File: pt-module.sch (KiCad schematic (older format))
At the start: 0 parts

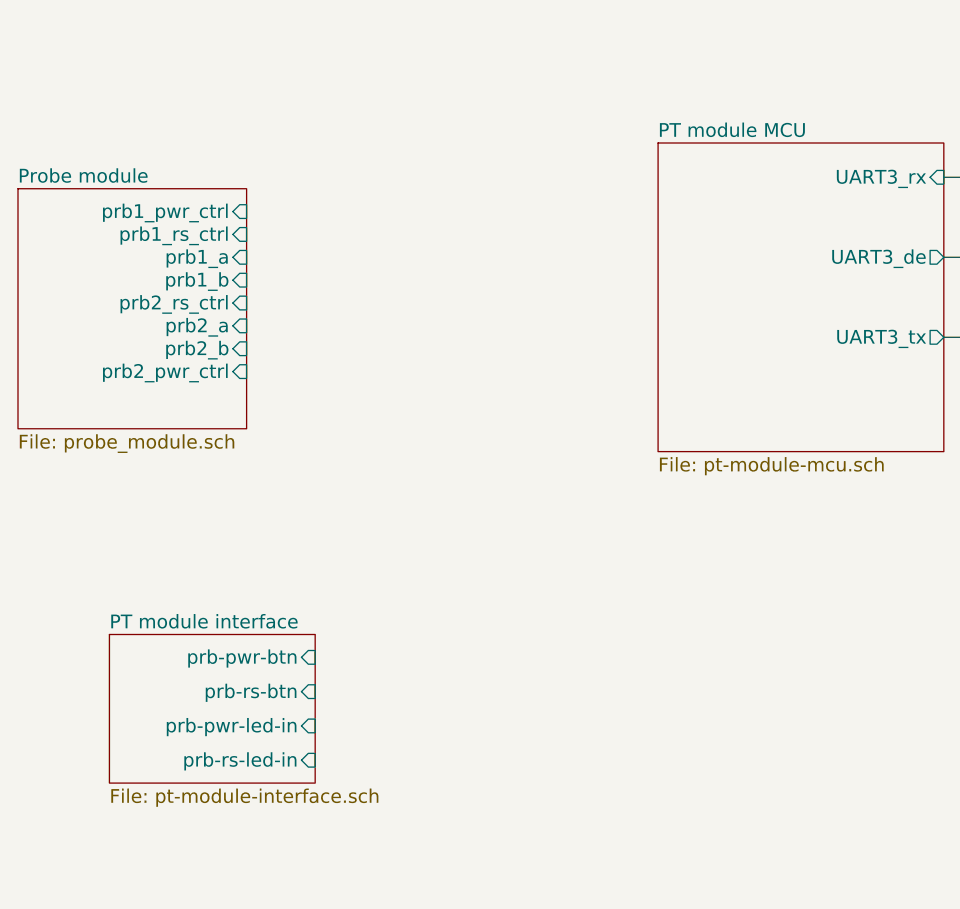
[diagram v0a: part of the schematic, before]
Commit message: add vaisala bus
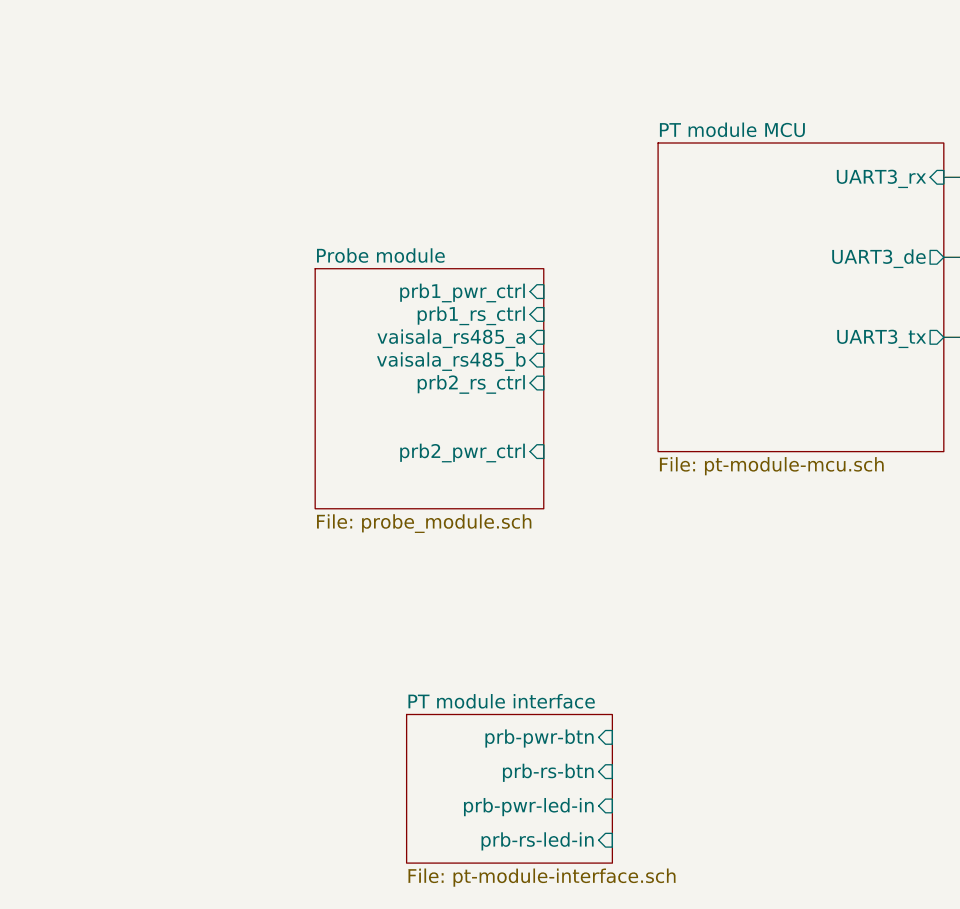
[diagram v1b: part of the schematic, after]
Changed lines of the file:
@@
 	6500 2100 7200 2100
 $Sheet
-S 1300 3000 1000 1050
+S 2600 3350 1000 1050
 U 598183C5
 F0 "Probe module" 60
 F1 "probe_module.sch" 60
-F2 "prb1_pwr_ctrl" I R 2300 3100 60
-F3 "prb1_rs_ctrl" I R 2300 3200 60
-F4 "prb1_a" I R 2300 3300 60
-F5 "prb1_b" I R 2300 3400 60
-F6 "prb2_rs_ctrl" I R 2300 3500 60
-F7 "prb2_a" I R 2300 3600 60
-F8 "prb2_b" I R 2300 3700 60
-F9 "prb2_pwr_ctrl" I R 2300 3800 60
+F2 "prb1_pwr_ctrl" I R 3600 3450 60
+F3 "prb1_rs_ctrl" I R 3600 3550 60
+F4 "prb2_rs_ctrl" I R 3600 3850 60
+F5 "prb2_pwr_ctrl" I R 3600 4150 60
+F6 "vaisala_rs485_a" I R 3600 3650 60
+F7 "vaisala_rs485_b" I R 3600 3750 60
 $EndSheet
 $Sheet
-S 1700 4950 900  650
+S 3000 5300 900  650
 U 59819805
 F0 "PT module interface" 60
 F1 "pt-module-interface.sch" 60
-F2 "prb-pwr-btn" I R 2600 5050 60
-F3 "prb-rs-btn" I R 2600 5200 60
-F4 "prb-pwr-led-in" I R 2600 5350 60
-F5 "prb-rs-led-in" I R 2600 5500 60
+F2 "prb-pwr-btn" I R 3900 5400 60
+F3 "prb-rs-btn" I R 3900 5550 60
+F4 "prb-pwr-led-in" I R 3900 5700 60
+F5 "prb-rs-led-in" I R 3900 5850 60
 $EndSheet
 $EndSCHEMATC

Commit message: add connectors
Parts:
- added J?: M12 out, symbol CONN_01X05
- added J? (x2): Ethercon out, symbol CONN_01X08
- added J?: M12 in, symbol CONN_01X05
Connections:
- new net GND: J?.2 (P2), J?.2 (P2), J?.8 (P8), J?.8 (P8)
- new net VCC: J?.1 (P1), J?.1 (P1), J?.1 (P1), J?.1 (P1), J?.2 (P2), J?.2 (P2), J?.3 (P3), J?.3 (P3)
- new net intermodule_rs485_a: J?.6 (P6), J?.6 (P6)
- new net intermodule_rs485_b: J?.7 (P7), J?.7 (P7)
- new net vaisala_rs485_a: J?.3 (P3), J?.3 (P3), J?.4 (P4), J?.4 (P4)
- new net vaisala_rs485_b: J?.4 (P4), J?.4 (P4), J?.5 (P5), J?.5 (P5)
- no-connect marks 0 -> 2
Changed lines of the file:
@@
 $EndDescr
 $Sheet
-S 7150 3350 1750 900
+S 2150 1200 1750 900
 U 5979DB00
 F0 "PT Module Power" 60
 F1 "pt-module-power.sch" 60
-F2 "PWREN" I L 7150 3625 60
+F2 "PWREN" I L 2150 1475 60
 $EndSheet
 $Sheet
@@
 F5 "prb-rs-led-in" I R 3900 5850 60
 $EndSheet
+$Comp
+L CONN_01X05 J?
+U 1 1 59820FE7
+P 10850 1050
+F 0 "J?" H 10850 1350 50  0000 C CNN
+F 1 "M12 out" V 10950 1050 50  0000 C CNN
+F 2 "" H 10850 1050 50  0001 C CNN
+F 3 "" H 10850 1050 50  0001 C CNN
+	1    10850 1050
+	1    0    0    -1
+$EndComp
+$Comp
+L VCC #PWR?
+U 1 1 598232AF
+P 10650 850
+F 0 "#PWR?" H 10650 700 50  0001 C CNN
+F 1 "VCC" H 10650 1000 50  0000 C CNN
+F 2 "" H 10650 850 50  0001 C CNN
+F 3 "" H 10650 850 50  0001 C CNN
+	1    10650 850
+	0    -1   -1   0
+$EndComp
+$Comp
+L GND #PWR?
+U 1 1 59823366
+P 10650 950
+F 0 "#PWR?" H 10650 700 50  0001 C CNN
+F 1 "GND" H 10650 800 50  0000 C CNN
+F 2 "" H 10650 950 50  0001 C CNN
+F 3 "" H 10650 950 50  0001 C CNN
+	1    10650 950
+	0    1    1    0
+$EndComp
+Text Label 10650 1050 2    60   ~ 0
+vaisala_rs485_a
+Text Label 10650 1150 2    60   ~ 0
+vaisala_rs485_b
+NoConn ~ 10650 1250
+$Comp
+L CONN_01X08 J?
+U 1 1 59829448
+P 10850 1900
+F 0 "J?" H 10850 2350 50  0000 C CNN
+F 1 "Ethercon out" V 10950 1900 50  0000 C CNN
+F 2 "" H 10850 1900 50  0001 C CNN
+F 3 "" H 10850 1900 50  0001 C CNN
+	1    10850 1900
+	1    0    0    -1
+$EndComp
+$Comp
+L CONN_01X05 J?
+U 1 1 5982A52D
+P 800 1250
+F 0 "J?" H 800 1550 50  0000 C CNN
+F 1 "M12 in" V 900 1250 50  0000 C CNN
+F 2 "" H 800 1250 50  0001 C CNN
+F 3 "" H 800 1250 50  0001 C CNN
+	1    800  1250
+	-1   0    0    1
+$EndComp
+$Comp
+L VCC #PWR?
+U 1 1 5982A533
+P 1000 1450
+F 0 "#PWR?" H 1000 1300 50  0001 C CNN
+F 1 "VCC" H 1000 1600 50  0000 C CNN
+F 2 "" H 1000 1450 50  0001 C CNN
+F 3 "" H 1000 1450 50  0001 C CNN
+	1    1000 1450
+	0    1    1    0
+$EndComp
+$Comp
+L GND #PWR?
+U 1 1 5982A539
+P 1000 1350
+F 0 "#PWR?" H 1000 1100 50  0001 C CNN
+F 1 "GND" H 1000 1200 50  0000 C CNN
+F 2 "" H 1000 1350 50  0001 C CNN
+F 3 "" H 1000 1350 50  0001 C CNN
+	1    1000 1350
+	0    -1   -1   0
+$EndComp
+Text Label 1000 1250 0    60   ~ 0
+vaisala_rs485_a
+Text Label 1000 1150 0    60   ~ 0
+vaisala_rs485_b
+NoConn ~ 1000 1050
+$Comp
+L VCC #PWR?
+U 1 1 59839AE4
+P 10650 1550
+F 0 "#PWR?" H 10650 1400 50  0001 C CNN
+F 1 "VCC" H 10650 1700 50  0000 C CNN
+F 2 "" H 10650 1550 50  0001 C CNN
+F 3 "" H 10650 1550 50  0001 C CNN
+	1    10650 1550
+	0    -1   -1   0
+$EndComp
+$Comp
+L GND #PWR?
+U 1 1 59839B9A
+P 10650 2250
+F 0 "#PWR?" H 10650 2000 50  0001 C CNN
+F 1 "GND" H 10650 2100 50  0000 C CNN
+F 2 "" H 10650 2250 50  0001 C CNN
+F 3 "" H 10650 2250 50  0001 C CNN
+	1    10650 2250
+	0    1    1    0
+$EndComp
+Text Label 10650 1850 2    60   ~ 0
+vaisala_rs485_a
+Text Label 10650 1950 2    60   ~ 0
+vaisala_rs485_b
+Text Label 10650 2050 2    60   ~ 0
+intermodule_rs485_a
+Text Label 10650 2150 2    60   ~ 0
+intermodule_rs485_b
+$Comp
+L VCC #PWR?
+U 1 1 5983E741
+P 10650 1650
+F 0 "#PWR?" H 10650 1500 50  0001 C CNN
+F 1 "VCC" H 10650 1800 50  0000 C CNN
+F 2 "" H 10650 1650 50  0001 C CNN
+F 3 "" H 10650 1650 50  0001 C CNN
+	1    10650 1650
+	0    -1   -1   0
+$EndComp
+$Comp
+L VCC #PWR?
+U 1 1 5983E7F1
+P 10650 1750
+F 0 "#PWR?" H 10650 1600 50  0001 C CNN
+F 1 "VCC" H 10650 1900 50  0000 C CNN
+F 2 "" H 10650 1750 50  0001 C CNN
+F 3 "" H 10650 1750 50  0001 C CNN
+	1    10650 1750
+	0    -1   -1   0
+$EndComp
+$Comp
+L CONN_01X08 J?
+U 1 1 59840D9B
+P 800 2200
+F 0 "J?" H 800 2650 50  0000 C CNN
+F 1 "Ethercon out" V 900 2200 50  0000 C CNN
+F 2 "" H 800 2200 50  0001 C CNN
+F 3 "" H 800 2200 50  0001 C CNN
+	1    800  2200
+	-1   0    0    1
+$EndComp
+$Comp
+L VCC #PWR?
+U 1 1 59840DA1
+P 1000 2550
+F 0 "#PWR?" H 1000 2400 50  0001 C CNN
+F 1 "VCC" H 1000 2700 50  0000 C CNN
+F 2 "" H 1000 2550 50  0001 C CNN
+F 3 "" H 1000 2550 50  0001 C CNN
+	1    1000 2550
+	0    1    1    0
+$EndComp
+$Comp
+L GND #PWR?
+U 1 1 59840DA7
+P 1000 1850
+F 0 "#PWR?" H 1000 1600 50  0001 C CNN
+F 1 "GND" H 1000 1700 50  0000 C CNN
+F 2 "" H 1000 1850 50  0001 C CNN
+F 3 "" H 1000 1850 50  0001 C CNN
+	1    1000 1850
+	0    -1   -1   0
+$EndComp
+Text Label 1000 2250 0    60   ~ 0
+vaisala_rs485_a
+Text Label 1000 2150 0    60   ~ 0
+vaisala_rs485_b
+Text Label 1000 2050 0    60   ~ 0
+intermodule_rs485_a
+Text Label 1000 1950 0    60   ~ 0
+intermodule_rs485_b
+$Comp
+L VCC #PWR?
+U 1 1 59840DB1
+P 1000 2450
+F 0 "#PWR?" H 1000 2300 50  0001 C CNN
+F 1 "VCC" H 1000 2600 50  0000 C CNN
+F 2 "" H 1000 2450 50  0001 C CNN
+F 3 "" H 1000 2450 50  0001 C CNN
+	1    1000 2450
+	0    1    1    0
+$EndComp
+$Comp
+L VCC #PWR?
+U 1 1 59840DB7
+P 1000 2350
+F 0 "#PWR?" H 1000 2200 50  0001 C CNN
+F 1 "VCC" H 1000 2500 50  0000 C CNN
+F 2 "" H 1000 2350 50  0001 C CNN
+F 3 "" H 1000 2350 50  0001 C CNN
+	1    1000 2350
+	0    1    1    0
+$EndComp
 $EndSCHEMATC

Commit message: add power connections
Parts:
- added J?: PWR in, symbol CONN_01X02
- added SW?: pwr-source switch, symbol SW_DPDT_x2
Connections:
- net GND: now also J?.1 (P1)
- net VCC: now also SW?.2 (B); no longer J?.1 (P1), J?.2 (P2), J?.3 (P3)
- new net E_VCC: SW?.1 (A)
- new net VDD: J?.2 (P2)
- new net VEE: J?.1 (P1), J?.2 (P2), J?.3 (P3), SW?.3 (C)
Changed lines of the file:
@@
 F1 "pt-module-power.sch" 60
 F2 "PWREN" I L 2150 1475 60
+F3 "External_VCC" I L 2150 2000 60
 $EndSheet
 $Sheet
@@
 F4 "UART3_de" O R 5350 3300 60
 $EndSheet
-Wire Wire Line
-	5350 3300 6200 3300
-Wire Wire Line
-	6200 3300 6200 1950
-Wire Wire Line
-	6200 1950 7200 1950
-Wire Wire Line
-	5350 2950 6000 2950
-Wire Wire Line
-	6000 2950 6000 1650
-Wire Wire Line
-	6000 1650 7200 1650
-Wire Wire Line
-	5350 3650 6500 3650
-Wire Wire Line
-	6500 3650 6500 2100
-Wire Wire Line
-	6500 2100 7200 2100
 $Sheet
 S 2600 3350 1000 1050
@@
 $EndComp
 $Comp
-L VCC #PWR?
-U 1 1 59840DA1
-P 1000 2550
-F 0 "#PWR?" H 1000 2400 50  0001 C CNN
-F 1 "VCC" H 1000 2700 50  0000 C CNN
-F 2 "" H 1000 2550 50  0001 C CNN
-F 3 "" H 1000 2550 50  0001 C CNN
-	1    1000 2550
-	0    1    1    0
-$EndComp
-$Comp
 L GND #PWR?
 U 1 1 59840DA7
@@
 intermodule_rs485_b
 $Comp
-L VCC #PWR?
-U 1 1 59840DB1
+L CONN_01X02 J?
+U 1 1 5984EE28
+P 800 3050
+F 0 "J?" H 800 3200 50  0000 C CNN
+F 1 "PWR in" V 900 3050 50  0000 C CNN
+F 2 "" H 800 3050 50  0001 C CNN
+F 3 "" H 800 3050 50  0001 C CNN
+	1    800  3050
+	-1   0    0    1
+$EndComp
+$Comp
+L GND #PWR?
+U 1 1 5984F347
+P 1000 3100
+F 0 "#PWR?" H 1000 2850 50  0001 C CNN
+F 1 "GND" H 1000 2950 50  0000 C CNN
+F 2 "" H 1000 3100 50  0001 C CNN
+F 3 "" H 1000 3100 50  0001 C CNN
+	1    1000 3100
+	0    -1   -1   0
+$EndComp
+$Comp
+L VDD #PWR?
+U 1 1 5984F4B5
+P 1000 3000
+F 0 "#PWR?" H 1000 2850 50  0001 C CNN
+F 1 "VDD" H 1000 3150 50  0000 C CNN
+F 2 "" H 1000 3000 50  0001 C CNN
+F 3 "" H 1000 3000 50  0001 C CNN
+	1    1000 3000
+	0    1    1    0
+$EndComp
+$Comp
+L SW_DPDT_x2 SW?
+U 1 1 5985369A
+P 1950 2700
+F 0 "SW?" H 1950 2870 50  0000 C CNN
+F 1 "pwr-source switch" H 1950 2500 50  0000 C CNN
+F 2 "" H 1950 2700 50  0001 C CNN
+F 3 "" H 1950 2700 50  0001 C CNN
+	1    1950 2700
+	-1   0    0    1
+$EndComp
+Wire Wire Line
+	5350 3300 6200 3300
+Wire Wire Line
+	6200 3300 6200 1950
+Wire Wire Line
+	6200 1950 7200 1950
+Wire Wire Line
+	5350 2950 6000 2950
+Wire Wire Line
+	6000 2950 6000 1650
+Wire Wire Line
+	6000 1650 7200 1650
+Wire Wire Line
+	5350 3650 6500 3650
+Wire Wire Line
+	6500 3650 6500 2100
+Wire Wire Line
+	6500 2100 7200 2100
+Text Label 2150 2000 0    60   ~ 0
+E_VCC
+Text Label 1750 2800 2    60   ~ 0
+E_VCC
+$Comp
+L VEE #PWR?
+U 1 1 5985D30F
+P 1000 2350
+F 0 "#PWR?" H 1000 2200 50  0001 C CNN
+F 1 "VEE" H 1000 2500 50  0000 C CNN
+F 2 "" H 1000 2350 50  0001 C CNN
+F 3 "" H 1000 2350 50  0001 C CNN
+	1    1000 2350
+	0    1    1    0
+$EndComp
+$Comp
+L VEE #PWR?
+U 1 1 5985D3D5
 P 1000 2450
 F 0 "#PWR?" H 1000 2300 50  0001 C CNN
-F 1 "VCC" H 1000 2600 50  0000 C CNN
+F 1 "VEE" H 1000 2600 50  0000 C CNN
 F 2 "" H 1000 2450 50  0001 C CNN
 F 3 "" H 1000 2450 50  0001 C CNN
@@
 $EndComp
 $Comp
-L VCC #PWR?
-U 1 1 59840DB7
-P 1000 2350
-F 0 "#PWR?" H 1000 2200 50  0001 C CNN
-F 1 "VCC" H 1000 2500 50  0000 C CNN
-F 2 "" H 1000 2350 50  0001 C CNN
-F 3 "" H 1000 2350 50  0001 C CNN
-	1    1000 2350
-	0    1    1    0
-$EndComp
+L VEE #PWR?
+U 1 1 5985D494
+P 1000 2550
+F 0 "#PWR?" H 1000 2400 50  0001 C CNN
+F 1 "VEE" H 1000 2700 50  0000 C CNN
+F 2 "" H 1000 2550 50  0001 C CNN
+F 3 "" H 1000 2550 50  0001 C CNN
+	1    1000 2550
+	0    1    1    0
+$EndComp
+$Comp
+L VEE #PWR?
+U 1 1 5985D762
+P 1750 2600
+F 0 "#PWR?" H 1750 2450 50  0001 C CNN
+F 1 "VEE" H 1750 2750 50  0000 C CNN
+F 2 "" H 1750 2600 50  0001 C CNN
+F 3 "" H 1750 2600 50  0001 C CNN
+	1    1750 2600
+	0    -1   -1   0
+$EndComp
+$Comp
+L VCC #PWR?
+U 1 1 5985DA3D
+P 2150 2700
+F 0 "#PWR?" H 2150 2550 50  0001 C CNN
+F 1 "VCC" H 2150 2850 50  0000 C CNN
+F 2 "" H 2150 2700 50  0001 C CNN
+F 3 "" H 2150 2700 50  0001 C CNN
+	1    2150 2700
+	0    1    1    0
+$EndComp
